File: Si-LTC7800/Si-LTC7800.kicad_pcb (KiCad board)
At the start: 2 copper layers, 27 parts, among them Q1 DMP2045U-7, Q2 DMP2045U-7, U1 LTC7800HUDC_PBF

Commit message: Updated shematics
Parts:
- added C6: 100pF, Capacitor_SMD:C_0805_2012Metric_Pad1.18x1.45mm_HandSolder, F.Cu at (103.0, 96.0)
- added CinA-E1: ~, Capacitor_SMD:C_0805_2012Metric_Pad1.18x1.45mm_HandSolder, F.Cu at (107.8, 87.0)
- added CinA-E10: ~, Capacitor_SMD:C_0805_2012Metric_Pad1.18x1.45mm_HandSolder, F.Cu at (112.7, 96.0)
- added CinA-E11: ~, Capacitor_SMD:C_0805_2012Metric_Pad1.18x1.45mm_HandSolder, F.Cu at (117.5, 81.0)
- added CinA-E12: ~, Capacitor_SMD:C_0805_2012Metric_Pad1.18x1.45mm_HandSolder, F.Cu at (117.5, 84.0)
- added CinA-E13: ~, Capacitor_SMD:C_0805_2012Metric_Pad1.18x1.45mm_HandSolder, F.Cu at (117.5, 87.0)
- added CinA-E14: ~, Capacitor_SMD:C_0805_2012Metric_Pad1.18x1.45mm_HandSolder, F.Cu at (117.5, 90.0)
- added CinA-E2: ~, Capacitor_SMD:C_0805_2012Metric_Pad1.18x1.45mm_HandSolder, F.Cu at (107.8, 90.0)
- added CinA-E3: ~, Capacitor_SMD:C_0805_2012Metric_Pad1.18x1.45mm_HandSolder, F.Cu at (107.8, 93.0)
- added CinA-E4: ~, Capacitor_SMD:C_0805_2012Metric_Pad1.18x1.45mm_HandSolder, F.Cu at (107.8, 96.0)
- added CinA-E5: ~, Capacitor_SMD:C_0805_2012Metric_Pad1.18x1.45mm_HandSolder, F.Cu at (112.7, 81.0)
- added CinA-E6: ~, Capacitor_SMD:C_0805_2012Metric_Pad1.18x1.45mm_HandSolder, F.Cu at (112.7, 84.0)
- added CinA-E7: ~, Capacitor_SMD:C_0805_2012Metric_Pad1.18x1.45mm_HandSolder, F.Cu at (112.7, 87.0)
- added CinA-E8: ~, Capacitor_SMD:C_0805_2012Metric_Pad1.18x1.45mm_HandSolder, F.Cu at (112.7, 90.0)
- added CinA-E9: ~, Capacitor_SMD:C_0805_2012Metric_Pad1.18x1.45mm_HandSolder, F.Cu at (112.7, 93.0)
- added R7: 33kOhm, Resistor_SMD:R_0201_0603Metric_Pad0.64x0.40mm_HandSolder, F.Cu at (121.3, 90.9)
- added R9: 3.92kOhm, Resistor_SMD:R_0201_0603Metric_Pad0.64x0.40mm_HandSolder, F.Cu at (121.3, 92.6)
- C1: value 0.1uF -> 0.05uF
- C5: value 10pF -> 2.2uF
- R5: value 90.9kOhm -> 6.8kOhm
- R6: value 280kOhm -> 2.7kOhm
- moved BFET_VGS1 66.5 mm to (91.0, 104.9)
- moved TFET_VGS1 46.7 mm to (91.0, 109.0)
- moved U1 38.2 mm to (115.6, 110.8)
- moved VSource_IN1 35.8 mm to (94.8, 97.0)
- moved VSource_GND1 35.8 mm to (94.8, 85.3)
- moved CinB1 33.0 mm to (117.5, 93.0)
- moved Cout1 33.0 mm to (117.5, 96.0)
- moved Q2 32.5 mm to (120.1, 103.8)
- moved Q1 29.1 mm to (120.1, 99.7)
- moved CinA-1 28.9 mm to (107.8, 81.0)
- moved CinA-2 28.9 mm to (107.8, 84.0)
- moved TP_VOUT1 28.1 mm to (115.3, 105.1)
- moved TP_VIN1 27.6 mm to (115.3, 100.1)
- moved R1 25.8 mm to (121.3, 80.4)
- moved R2 25.8 mm to (121.3, 82.1)
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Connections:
- C5 pad 1: /SENSE- -> GND
- C5 pad 2: /VFB -> Net-(C5-Pad2)
- R6 pad 2: /VFB -> Net-(R6-Pad2)
- U1 pad 8: unconnected-(U1-ITH-Pad8) -> /ITH

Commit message: Si Schematic Update
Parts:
- removed CinA-E1, CinA-E2, CinA-E4, CinA-E5, CinA-E6: ~, Capacitor_SMD:C_0805_2012Metric_Pad1.18x1.45mm_HandSolder
- added Ex_Cin2: ~, Capacitor_SMD:C_0805_2012Metric_Pad1.18x1.45mm_HandSolder, F.Cu at (134.0, 124.0)
- BFET_VGS1, TFET_VGS1: footprint TestPoint:TestPoint_Bridge_Pitch2.54mm_Drill1.0mm -> TestPoint:TestPoint_2Pads_Pitch2.54mm_Drill0.8mm
- moved C4 64.2 mm to (154.0, 129.0)
- moved Ex_Cout2 62.8 mm to (158.0, 129.0), turned to 180 degrees
- moved R3 60.8 mm to (152.6, 136.0)
- moved R5 60.0 mm to (162.0, 131.4), turned to -90 degrees
- moved C3 59.5 mm to (132.0, 139.0)
- moved Ex_Cout1 59.1 mm to (158.0, 127.0), turned to 180 degrees
- moved R7 59.0 mm to (164.0, 131.6), turned to -90 degrees
- moved R4 58.5 mm to (152.6, 135.0)
- moved E_C4 56.1 mm to (154.0, 131.0), turned to 180 degrees
- moved TFET_VGS1 54.4 mm to (137.0, 138.0)
- moved RLoad1 54.4 mm to (157.4, 135.0)
- moved Cout1 53.5 mm to (158.0, 131.0)
- moved C2 53.1 mm to (138.0, 124.0), turned to -90 degrees
- moved C1 52.7 mm to (127.0, 128.0), turned to -90 degrees
- moved BFET_VGS1 52.7 mm to (141.5, 120.0)
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- renumbered CinA-1 to CinA1, CinA-2 to CinA2, CinA-E3 to E_C1, CinA-E7 to E_C2, CinA-E8 to E_C3, CinA-E9 to E_C4, CinA-E10 to E_C5, CinA-E13 to E_C6, CinA-E14 to Ex_Cin1, CinA-E12 to Ex_Cout1, CinA-E11 to Ex_Cout2
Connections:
- net /SENSE- renamed /Vout
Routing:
- net /SW: track 0.00 -> 11.6 mm
- net /VIN: track 0.00 -> 6.95 mm, vias 0 -> 2
- net /TG: track 0.00 -> 6.09 mm
- net GND: track 0.00 -> 3.68 mm, vias 0 -> 2
- net /BG: track 0.00 -> 3.33 mm

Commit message: ip
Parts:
- moved L1 41.4 mm to (165.9, 95.5)
- moved BFET_VGS1 41.4 mm to (161.1, 83.5)
- moved C4 41.4 mm to (173.6, 92.5)
- moved Cout1 41.4 mm to (177.6, 94.5)
- moved D1 41.4 mm to (162.6, 87.5)
- moved E_C4 41.4 mm to (173.6, 94.5)
- moved Ex_Cout1 41.4 mm to (177.7, 90.5)
- moved Ex_Cout2 41.4 mm to (177.6, 92.5)
- moved R3 41.4 mm to (172.2, 99.5)
- moved R4 41.4 mm to (172.2, 98.5)
- moved R5 41.4 mm to (181.6, 94.9)
- moved R6 41.4 mm to (178.6, 88.5)
- moved RLoad1 41.4 mm to (177.0, 98.5)
- moved TP_VOUT1 41.4 mm to (170.6, 85.5)
- moved R7 41.4 mm to (183.6, 95.1)
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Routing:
- net /SW: track 11.6 -> 0.23 mm
- net /VIN: track 6.95 -> 0.00 mm, vias 2 -> 0
- net /TG: track 6.09 -> 0.00 mm
- net GND: track 3.68 -> 0.00 mm, vias 2 -> 0
- net /BG: track 3.33 -> 0.00 mm

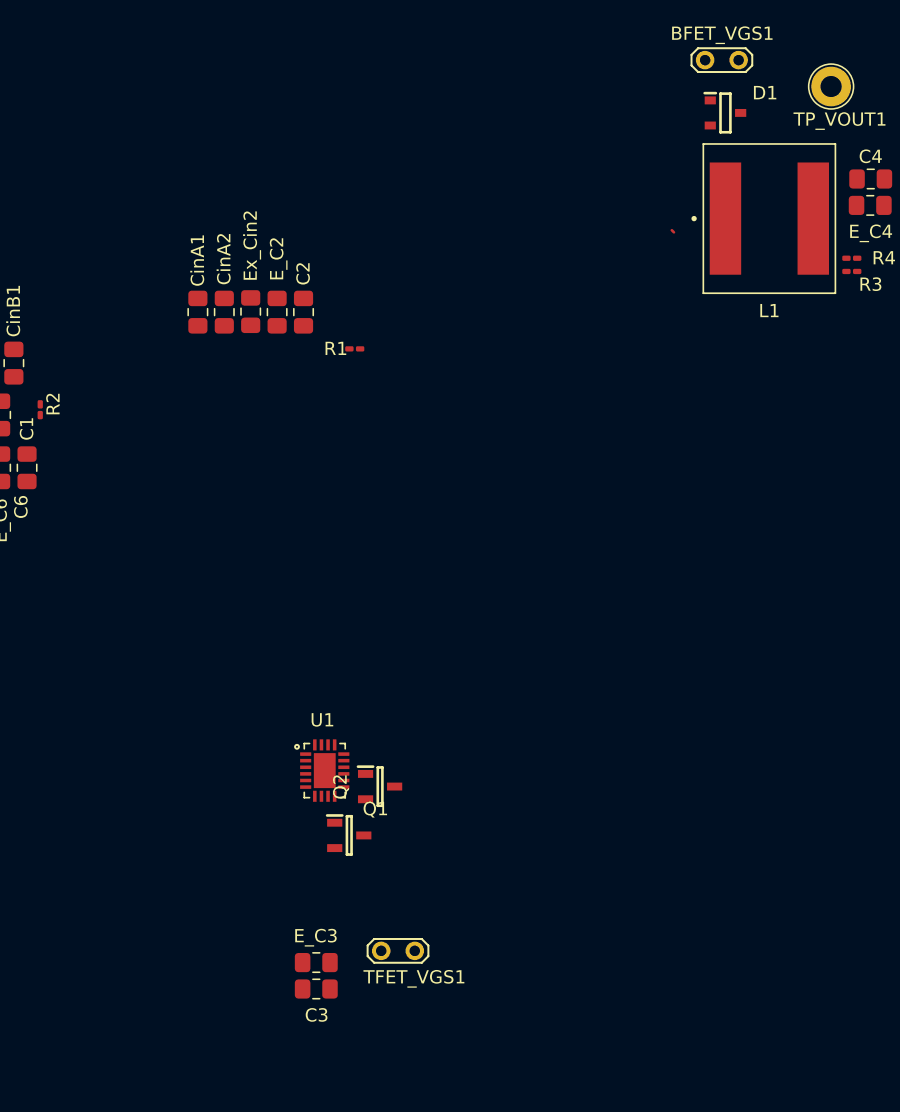
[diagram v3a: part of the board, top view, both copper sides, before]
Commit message: FET fixes
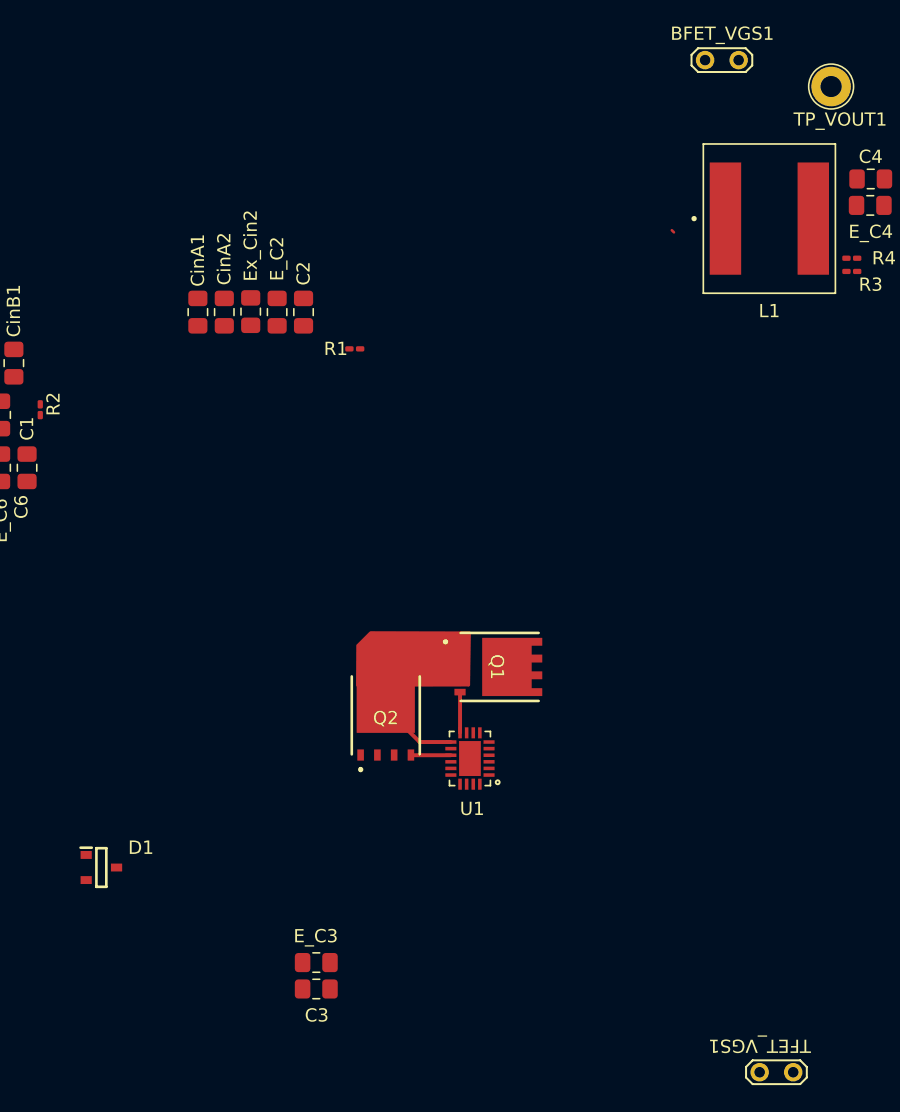
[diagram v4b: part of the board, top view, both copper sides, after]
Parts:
- Q1, Q2: value DMP2045U-7 -> BSC100N06LS3_G; footprint Transistor_Power:SOT96P240X115-3N -> XT60PW-M:BSC100N06LS3G
- moved D1 74.1 mm to (115.4, 144.6)
- moved TFET_VGS1 32.5 mm to (167.7, 160.1), turned to 180 degrees
- moved Q1 15.3 mm to (142.5, 129.4), turned to -90 degrees
- moved U1 11.0 mm to (143.3, 136.4), turned to 180 degrees
- moved Q2 2.43 mm to (136.9, 136.1)
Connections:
- Q1 pad 1: /TG -> /SW
- Q1 pad 3: /VIN -> /SW
- Q2 pad 1: /BG -> GND
- Q2 pad 3: /SW -> GND
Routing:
- net /SW: track 0.23 -> 6.22 mm
- net /TG: track 0.00 -> 3.08 mm
- net /BG: track 0.00 -> 3.03 mm

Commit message: fixing flip issue
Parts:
- D1: moved to B.Cu
- moved D1 25.4 mm to (139.5, 136.5), turned to 90 degrees
- moved C3 19.1 mm to (131.9, 134.7), turned to 90 degrees
- moved E_C3 17.2 mm to (129.9, 134.7), turned to -90 degrees
- moved Q2 0.31 mm to (136.6, 136.1)
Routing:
- net /BOOST: track 0.00 -> 12.0 mm, vias 0 -> 2
- net /BG: track 3.03 -> 3.65 mm

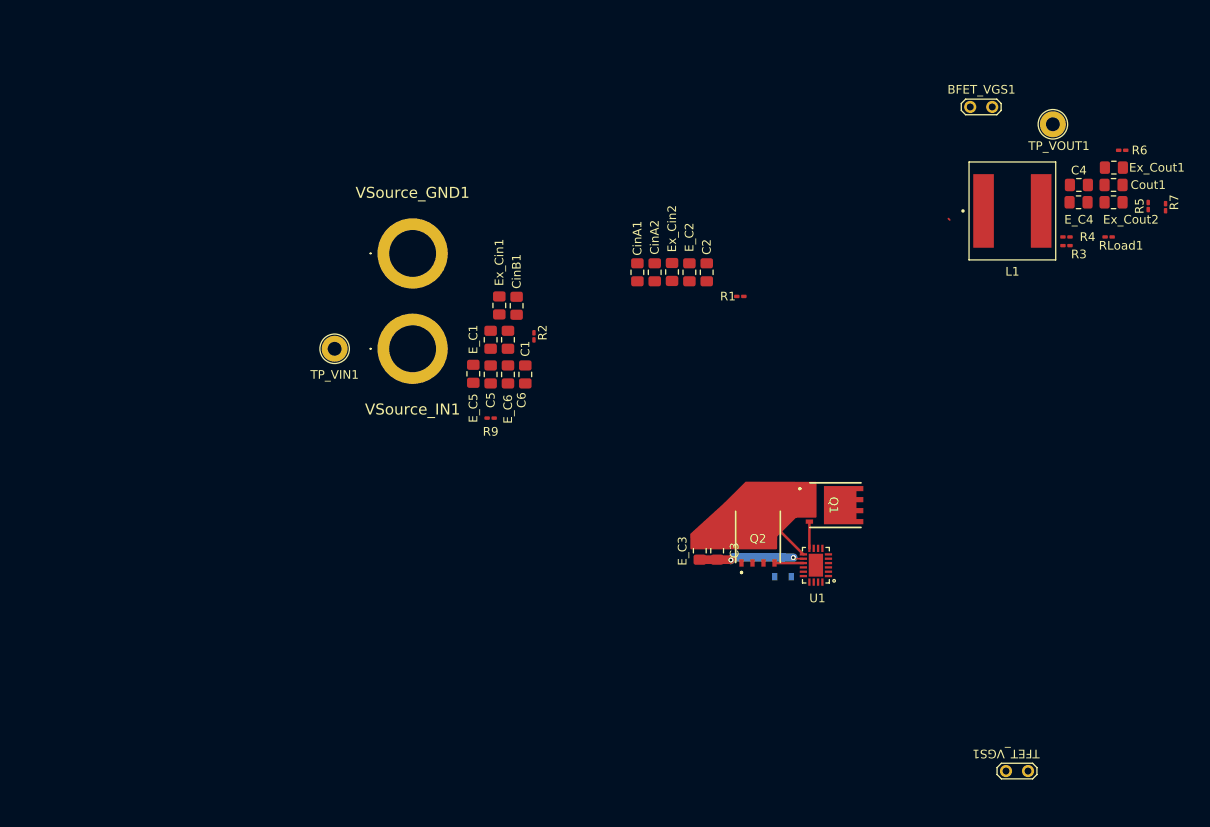
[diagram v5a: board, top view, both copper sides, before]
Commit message: Finished draft of GaN PCB
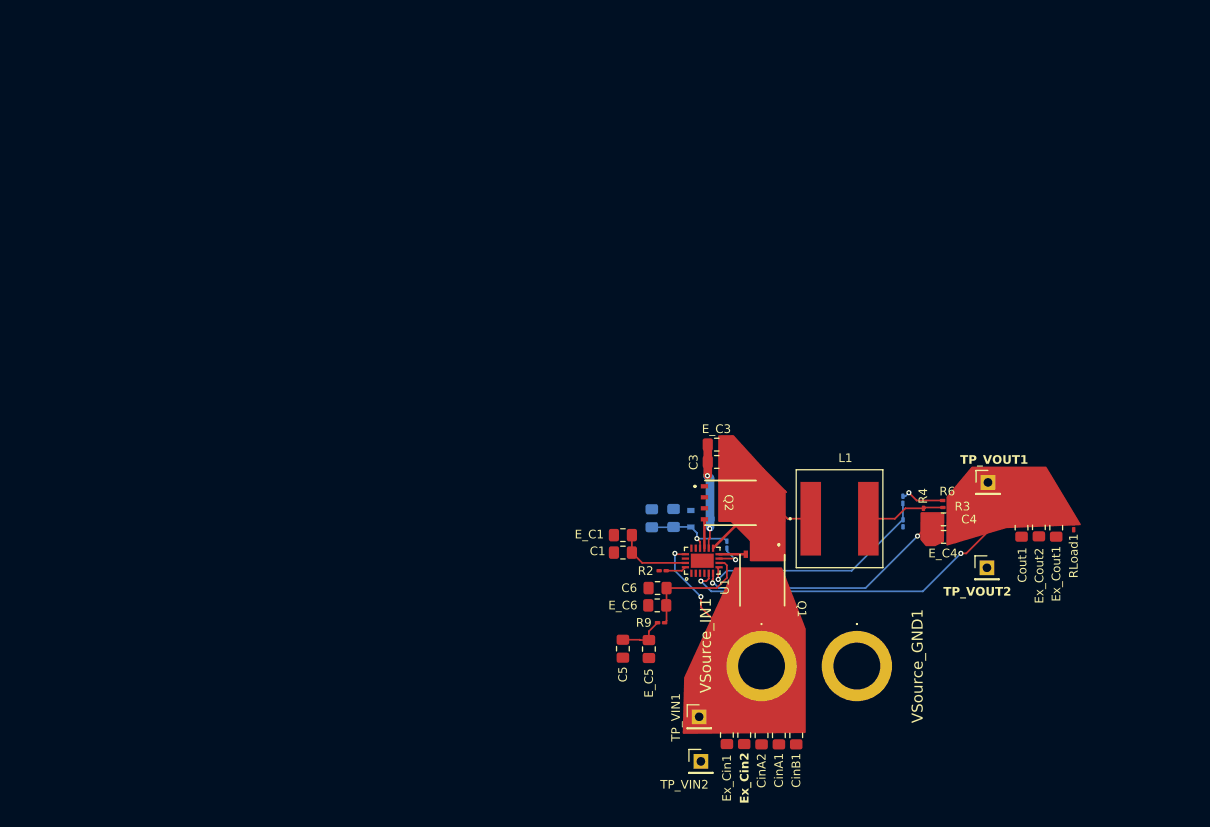
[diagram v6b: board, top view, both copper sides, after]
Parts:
- removed BFET_VGS1, TFET_VGS1: TestPoint_2Pole, TestPoint:TestPoint_2Pads_Pitch2.54mm_Drill0.8mm
- added TP_VIN2: ~, Connector_PinHeader_2.54mm:PinHeader_1x01_P2.54mm_Vertical, F.Cu at (130.0, 159.0)
- added TP_VOUT2: ~, Connector_PinHeader_2.54mm:PinHeader_1x01_P2.54mm_Vertical, F.Cu at (163.0, 136.7)
- C2, E_C2, R1, R5, R7: moved to B.Cu
- TP_VIN1, TP_VOUT1: value TestPoint -> ~; footprint TestPoint:TestPoint_Loop_D2.60mm_Drill1.6mm_Beaded -> Connector_PinHeader_2.54mm:PinHeader_1x01_P2.54mm_Vertical
- moved VSource_GND1 70.0 mm to (148.0, 148.0), turned to -90 degrees
- moved TP_VIN1 59.8 mm to (129.8, 153.9)
- moved CinB1 59.1 mm to (141.0, 156.0), turned to -90 degrees
- moved Ex_Cin1 56.1 mm to (133.0, 156.0), turned to -90 degrees
- moved CinA1 55.9 mm to (139.0, 156.0), turned to -90 degrees
- moved CinA2 54.8 mm to (137.0, 156.0), turned to -90 degrees
- moved VSource_IN1 54.4 mm to (137.0, 148.0), turned to -90 degrees
- moved Ex_Cin2 54.1 mm to (135.0, 156.0), turned to 90 degrees
- moved R5 46.3 mm to (153.3, 131.5)
- moved R7 45.4 mm to (153.3, 128.8)
- moved R6 45.2 mm to (158.3, 128.9), turned to 180 degrees
- moved Ex_Cout1 42.1 mm to (171.0, 132.0), turned to 90 degrees
- moved TP_VOUT1 42.0 mm to (163.1, 126.8)
- moved E_C4 41.6 mm to (158.0, 133.1)
- moved C4 41.6 mm to (158.0, 131.1)
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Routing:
- net /Vout: track 0.00 -> 42.3 mm, vias 0 -> 2
- net /SENSE+: track 0.00 -> 29.6 mm, vias 0 -> 2
- net /VFB: track 0.00 -> 27.5 mm, vias 0 -> 1
- net /VIN: track 0.00 -> 15.8 mm, vias 0 -> 2
- net /ITH: track 0.00 -> 14.0 mm
- net /INTVCC: track 0.00 -> 11.0 mm, vias 0 -> 1
- net Net-(L1-Pad2): track 0.00 -> 9.14 mm
- net Net-(U1-TRACK/SS): track 0.00 -> 8.68 mm
- net Net-(C5-Pad2): track 0.00 -> 5.43 mm
- net /SW: track 6.53 -> 11.7 mm
- net Net-(R6-Pad2): track 0.00 -> 5.13 mm, vias 0 -> 1
- net Net-(U1-PGOOD): track 0.00 -> 3.69 mm, vias 0 -> 1
- net Net-(U1-FREQ): track 0.00 -> 2.38 mm

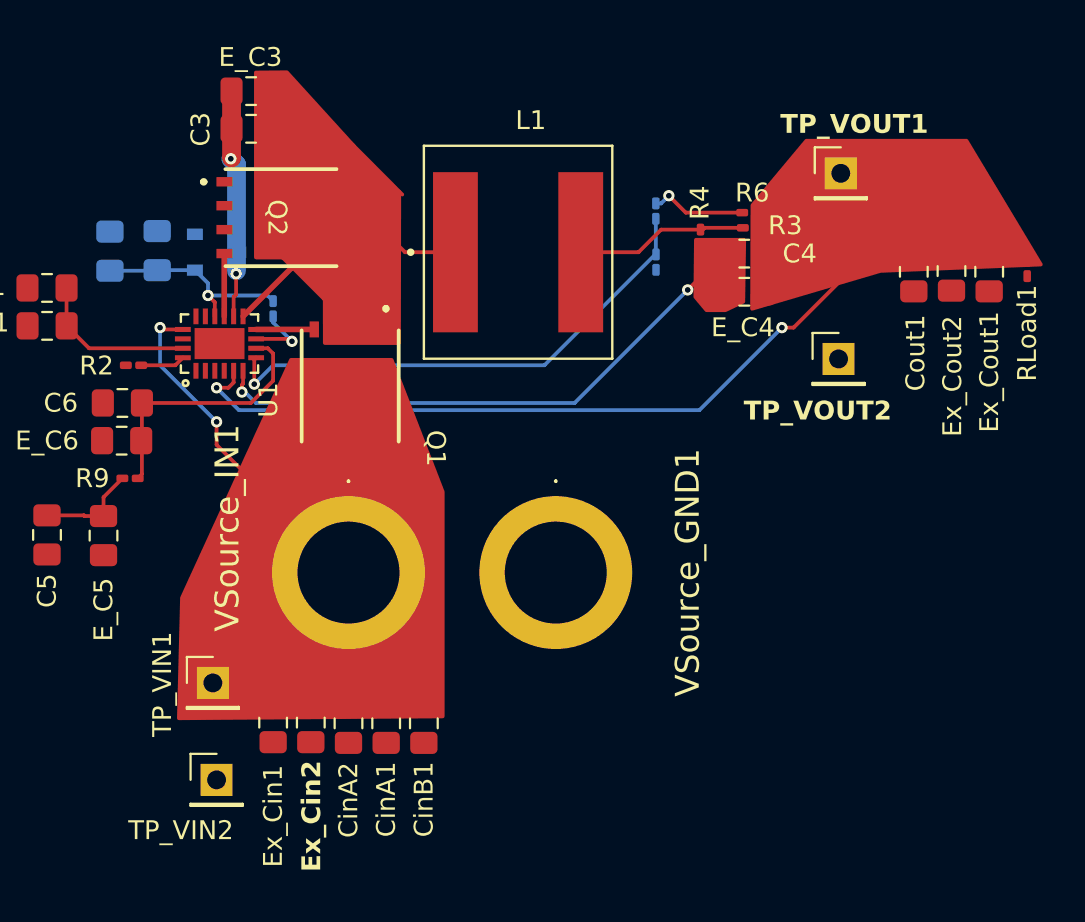
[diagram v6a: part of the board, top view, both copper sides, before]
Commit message: power traces sortof done
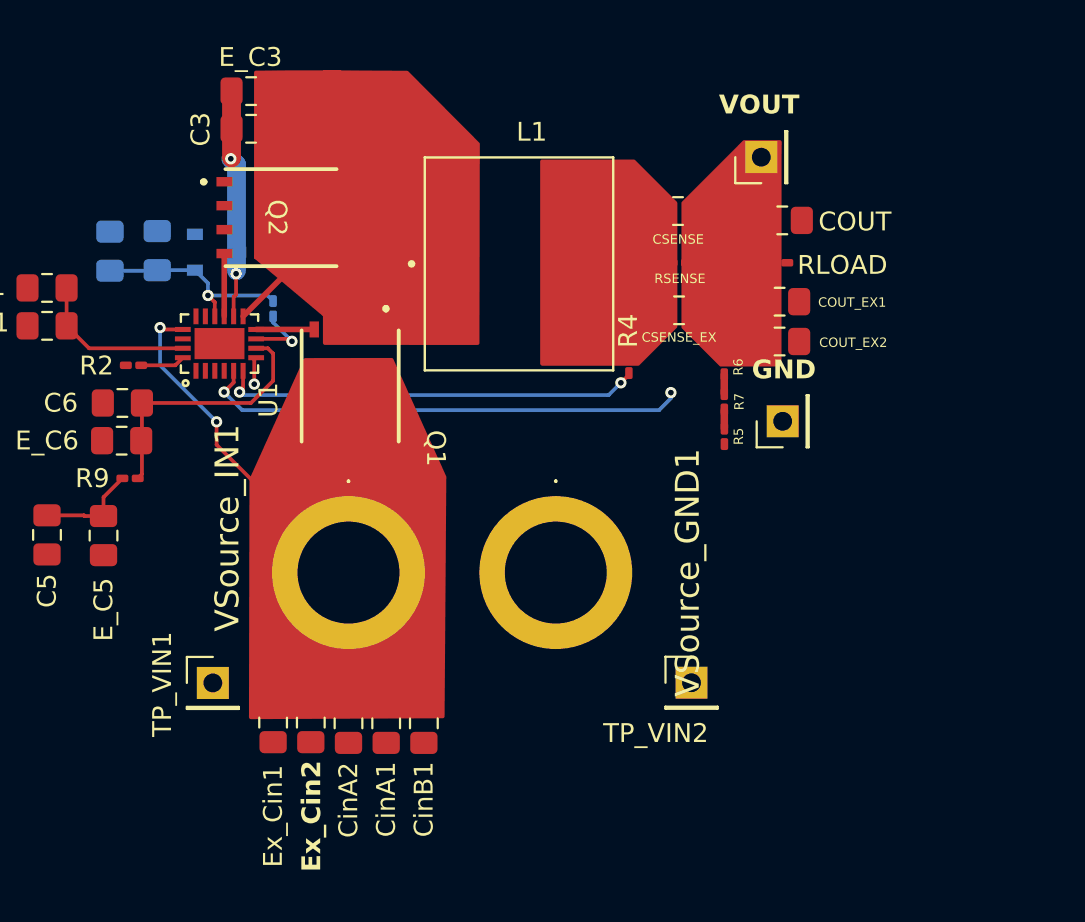
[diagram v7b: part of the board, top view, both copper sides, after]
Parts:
- R5, R7: moved to F.Cu
- moved TP_VIN2 25.7 mm to (155.2, 153.8)
- moved RLOAD 13.1 mm to (159.9, 131.6), turned to 0 degrees
- moved COUT_EX1 11.2 mm to (159.9, 133.6), turned to 180 degrees
- moved R7 10.8 mm to (156.9, 138.9)
- moved R5 9.93 mm to (156.9, 140.8)
- moved COUT_EX2 9.86 mm to (159.9, 135.7), turned to 180 degrees
- moved R6 8.28 mm to (156.9, 137.1), turned to -90 degrees
- moved R4 7.79 mm to (151.9, 137.0)
- moved COUT 7.49 mm to (160.0, 129.3), turned to 0 degrees
- moved GND 4.44 mm to (160.0, 140.0), turned to 90 degrees
- moved VOUT 4.31 mm to (158.9, 126.0), turned to 90 degrees
- moved RSENSE 4.21 mm to (154.6, 131.6)
- moved CSENSE 4.18 mm to (154.5, 128.8)
- moved CSENSE_EX 3.60 mm to (154.5, 134.1)
- moved L1 0.62 mm to (146.0, 131.6)
- renumbered Cout1 to COUT, Ex_Cout1 to COUT_EX1, Ex_Cout2 to COUT_EX2, C4 to CSENSE, E_C4 to CSENSE_EX, TP_VOUT2 to GND, RLoad1 to RLOAD, R3 to RSENSE, TP_VOUT1 to VOUT
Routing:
- net /VFB: track 27.5 -> 2.46 mm
- net /Vout: track 42.3 -> 26.0 mm
- net Net-(L1-Pad2): track 9.14 -> 0.00 mm
- net /SENSE+: track 29.6 -> 22.5 mm
- net /SW: track 11.7 -> 6.30 mm
- net Net-(R6-Pad2): track 5.13 -> 1.06 mm, vias 1 -> 0
